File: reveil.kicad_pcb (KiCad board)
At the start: 2 copper layers, 170 x 90 mm, 31 parts, among them J1 Barrel_Jack_Switch, J2 AudioJack3_SwitchTR, Q1 2N3904, Q2 IRF540N, U1 MAX7219, U2 MAX7219

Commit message: Mise à jour du layout PCB
Co-Authored-By: Claude Sonnet 5 <noreply@anthropic.com>
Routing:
- net ARRET_ALARME: track 166.8 -> 171.3 mm
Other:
- board text added: "+3V3"
- board text added: "ALARME_ON_OFF"
- board text added: "ARRET_ALARME"
- board text added: "DATE_CLK"
- board text added: "DATE_DIN"
- board text added: "DATE_LOAD"
- board text added: "GND"
- board text added: "H_ALRM_CLK"
- board text added: "H_ALRM_DIN"
- board text added: "H_ALRM_LD"
- board text added: "LED"
- board text added: "LUMIERE"
- board text added: "LUMINOSITE"
- board text added: "REG_ALRM_A"
- board text added: "REG_ALRM_B"
- board text added: "REG_ALRM_S"
- board text added: "REG_DATE_A"
- board text added: "REG_DATE_B"
- board text added: "REG_DATE_S"
- board text added: "REG_HR_A"
- board text added: "REG_HR_B"
- board text added: "REG_HR_S"
- board text added: "Réveil pour sourd Oscar Lederrey V1.1"
- board text added: "VBUS"
- board text added: "VIBREUR"
- board text removed: "Réveil pour sourd Oscar Lederrey V1.0"

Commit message: Corrige le pinout du footprint du switch ALARME_ON_OFF1 (court-circuit GND/+3V3)
Le footprint système Button_Switch_THT:SW_Slide-03_Wuerth-WS-SLTV a
les pads 1 et 2 physiquement inversés par rapport au composant monté
(pin 1 attendu à gauche, pin 2 au centre — le footprint avait
l'inverse). Résultat : selon la position du switch, +3V3 et GND se
retrouvaient court-circuités via l'interrupteur, faisant chauffer le
Pico et les câbles d'alimentation.

Correctif : nouvelle librairie locale reveil.pretty/ avec une copie
du footprint où seuls les pads 1 et 2 échangent leur géométrie (même
taille/forme/perçage, juste la position), enregistrée via
fp-lib-table. Le schéma (ALARME_ON_OFF1) et le PCB référencent
maintenant reveil:SW_Slide-03_... ; les pistes ont été reroutées en
conséquence.

Confirmé par :
- Mesure au multimètre (court quasi 0 Ω entre GND et +3V3, reproduit
  en rebranchant ces deux fils) ayant permis d'identifier la cause
- ERC propre (0 erreur/avertissement)
- DRC propre après routage (plus de shorting_items ni de pad non
  connecté sur ALARME_ON_OFF1)

Co-Authored-By: Claude Sonnet 5 <noreply@anthropic.com>
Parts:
- ALARME_ON_OFF1: footprint Button_Switch_THT:SW_Slide-03_Wuerth-WS-SLTV_10x2.5x6.4_P2.54mm -> reveil:SW_Slide-03_Wuerth-WS-SLTV_10x2.5x6.4_P2.54mm
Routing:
- net +3V3: track 171.7 -> 182.7 mm
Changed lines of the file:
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@@
 		)
 	)
-	(footprint "Button_Switch_THT:SW_Slide-03_Wuerth-WS-SLTV_10x2.5x6.4_P2.54mm"
+	(footprint "reveil:SW_Slide-03_Wuerth-WS-SLTV_10x2.5x6.4_P2.54mm"
 		(layer "F.Cu")
 		(at 196.46 90.5 180)
@@
 			)
 		)
-		(pad "1" thru_hole rect
-			(at 0 0 180)
-			(size 1.5 1.5)
+		(pad "1" thru_hole circle
+			(at -2.54 0 180)
+			(size 1.6 1.6)
 			(drill 0.8)
 			(layers "*.Cu" "*.Mask")
@@
 			(pintype "passive")
 		)
-		(pad "2" thru_hole circle
-			(at -2.54 0 180)
-			(size 1.6 1.6)
+		(pad "2" thru_hole rect
+			(at 0 0 180)
+			(size 1.5 1.5)
 			(drill 0.8)
 			(layers "*.Cu" "*.Mask")
@@
 	(segment
 		(start 197.321 88.821)
-		(end 199 90.5)
+		(end 196.46 90.5)
 		(width 0.2)
 		(layer "B.Cu")
@@
 	)
 	(segment
+		(start 191.4655 85.5055)
+		(end 191.4655 92.4655)
+		(width 0.2)
+		(layer "B.Cu")
+		(net 28)
+	)
+	(segment
 		(start 140.4925 85.1882)
 		(end 141.0978 85.7935)
@@
 	)
 	(segment
+		(start 193 94)
+		(end 198 94)
+		(width 0.2)
+		(layer "B.Cu")
+		(net 28)
+	)
+	(segment
 		(start 132.9578 59.1761)
 		(end 140.4925 66.7108)
@@
 	)
 	(segment
+		(start 191.4655 92.4655)
+		(end 193 94)
+		(width 0.2)
+		(layer "B.Cu")
+		(net 28)
+	)
+	(segment
 		(start 132.9578 55.2865)
 		(end 132.9578 59.1761)
@@
 	)
 	(segment
+		(start 199 93)
+		(end 199 90.5)
+		(width 0.2)
+		(layer "B.Cu")
+		(net 28)
+	)
+	(segment
 		(start 140.2231 37.2731)
 		(end 140.2231 48.0212)
@@
 	)
 	(segment
-		(start 140.4925 66.7108)
-		(end 140.4925 85.1882)
+		(start 198 94)
+		(end 199 93)
 		(width 0.2)
 		(layer "B.Cu")
@@
 	)
 	(segment
-		(start 140.2231 48.0212)
-		(end 132.9578 55.2865)
+		(start 140.4925 66.7108)
+		(end 140.4925 85.1882)
 		(width 0.2)
 		(layer "B.Cu")
@@
 	)
 	(segment
-		(start 191.4655 85.5055)
-		(end 196.46 90.5)
+		(start 140.2231 48.0212)
+		(end 132.9578 55.2865)
 		(width 0.2)
 		(layer "B.Cu")

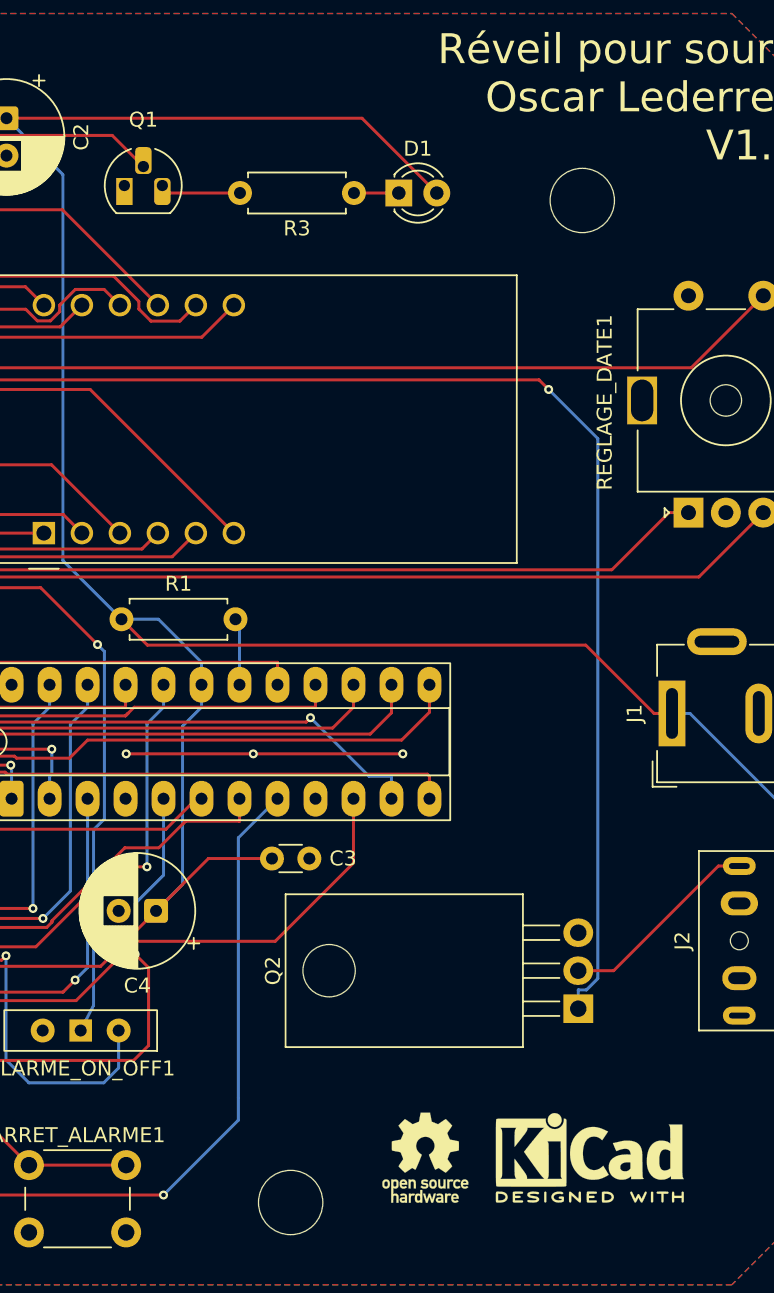
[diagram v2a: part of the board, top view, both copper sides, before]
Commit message: Place et route R4 sur le PCB (résistance de base LED)
R4 (1.5 kΩ, ajoutée au schéma dans le commit précédent) est
maintenant placée et routée sur le PCB. reveil.kicad_sch est
reformaté par KiCad (réordonnancement interne des blocs, aucun
changement électrique) suite à la synchronisation schéma/PCB.

Vérifié par ERC (0 erreur/avertissement) et DRC (0 pad non connecté,
0 erreur de footprint ; seuls restent des avertissements
silk_edge_clearance préexistants sur J2, sans rapport avec ce fix).

Test fonctionnel de la LED pas encore fait : une correction PCB
supplémentaire est nécessaire avant de pouvoir tester (voir TODO
README).

Co-Authored-By: Claude Sonnet 5 <noreply@anthropic.com>
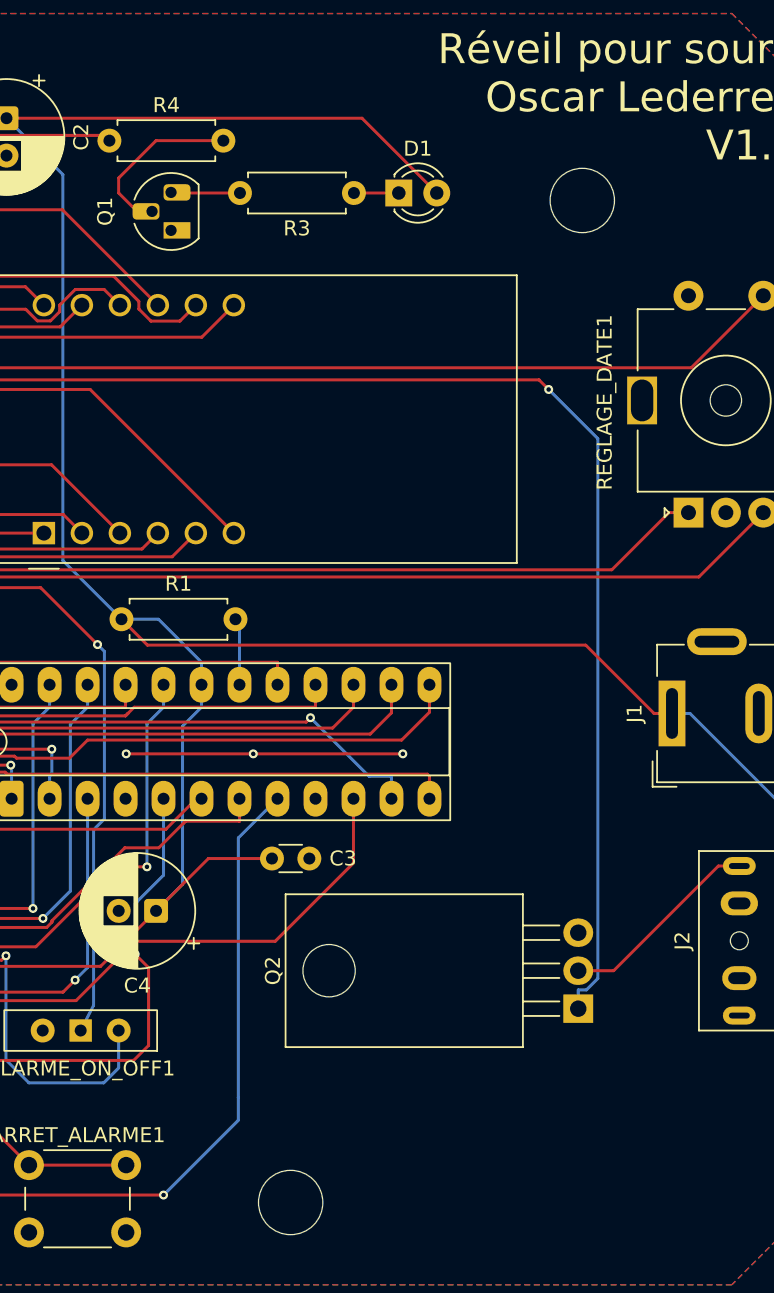
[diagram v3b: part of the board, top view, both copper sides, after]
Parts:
- removed LOGO1: OSHW-Logo_5.7x6mm_SilkScreen, Symbol:OSHW-Logo_5.7x6mm_SilkScreen
- removed LOGO2: KiCad-Logo2_5mm_SilkScreen, Symbol:KiCad-Logo2_5mm_SilkScreen
- added R4: 1.5K, Resistor_THT:R_Axial_DIN0207_L6.3mm_D2.5mm_P7.62mm_Horizontal, F.Cu at (198.4, 31.0)
- R3: value R -> 100
- moved Q1 4.33 mm to (202.5, 37.0), turned to 90 degrees
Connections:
- Q1 pad 2: LED -> Net-(Q1-B)
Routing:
- net Net-(Q1-B): track 0.00 -> 11.8 mm
- net LED: track 123.8 -> 120.8 mm
- net Net-(Q1-C): track 5.40 -> 4.63 mm

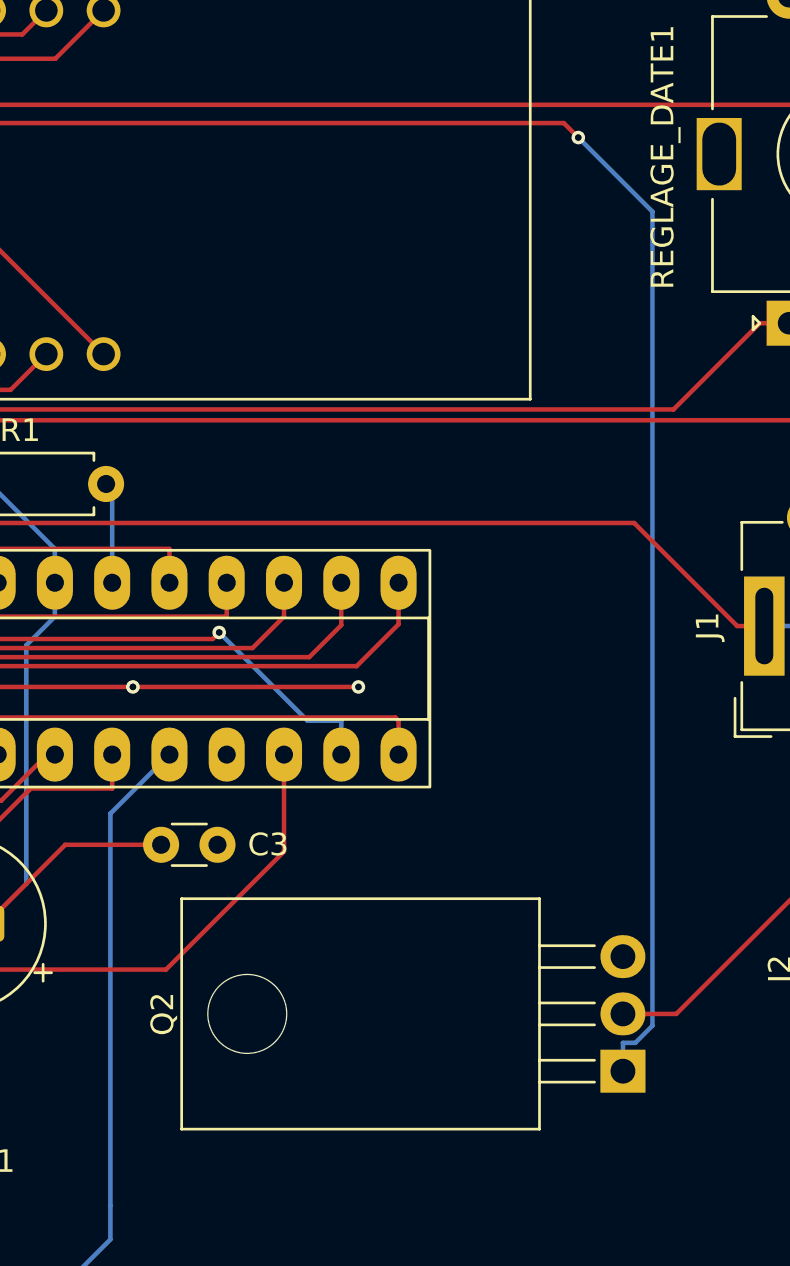
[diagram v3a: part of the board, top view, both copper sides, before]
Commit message: Remplace Q2 (IRF510/IRF540N) par un IRLB8721PbF logic-level et ajoute R5
Le RP2040 pilote la grille de Q2 directement en 3.3V (GP18), et ni
l'IRF510 (carte physique) ni l'IRF540N (schéma) ne sont des MOSFET
logic-level (Rds(on) specifie a Vgs=10V) : risque de sous-enhancement
et d'echauffement. L'IRLB8721PbF est pleinement enhance des 2.5-4.5V,
compatible avec un pilotage direct en 3.3V.

Ajoute R5 = 100 ohm en serie entre GP18 et la grille de Q2 pour
limiter le pic de courant transitoire et amortir le ringing.

Verifie : pinout G/D/S (broches 1/2/3, meme convention que l'IRF540N),
footprint TO-220-3_Horizontal_TabDown (corrige apres reperage d'un
TO-220F errone), ERC (0 violation) et DRC (6 avertissements
preexistants sur J2, sans rapport).

Co-Authored-By: Claude Sonnet 5 <noreply@anthropic.com>
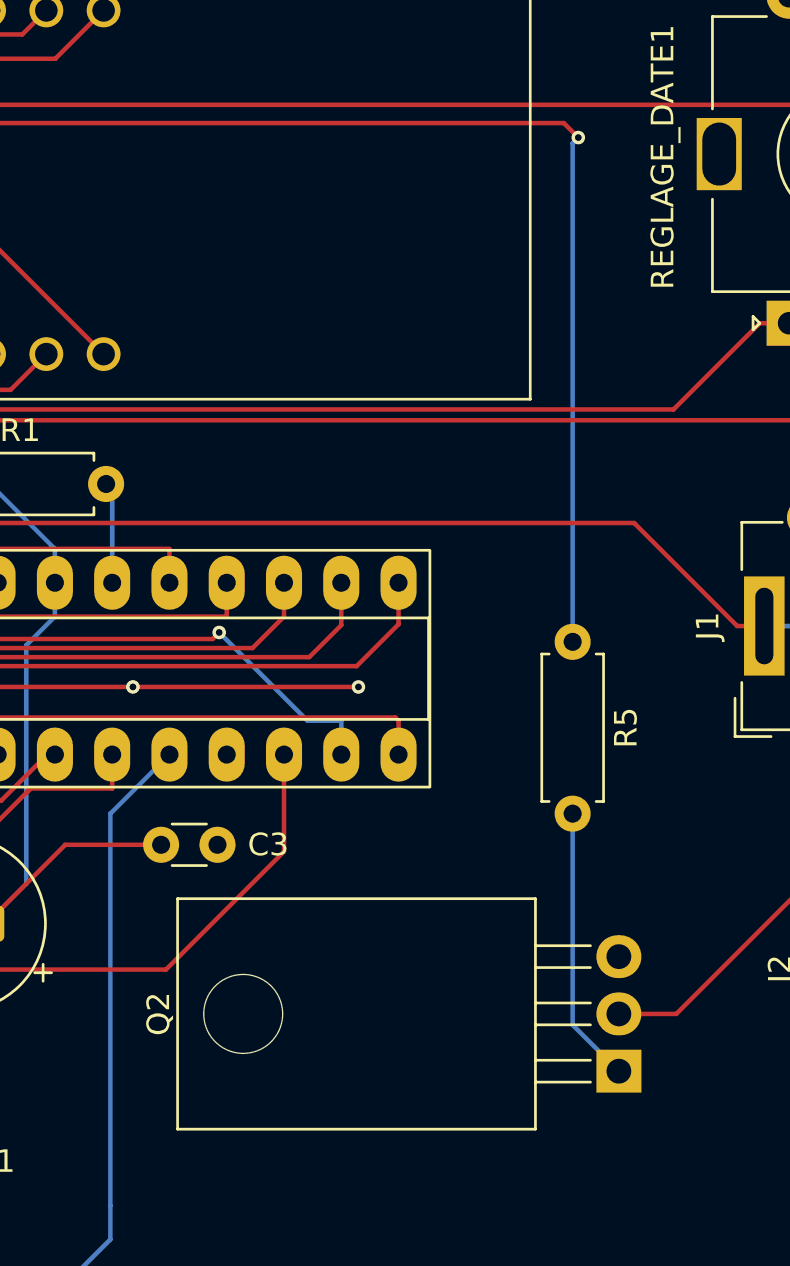
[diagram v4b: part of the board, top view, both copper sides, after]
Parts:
- added R5: 100R, Resistor_THT:R_Axial_DIN0207_L6.3mm_D2.5mm_P7.62mm_Horizontal, F.Cu at (227.5, 70.0)
- Q2: value IRF540N -> IRLB8721PBF
- moved Q2 0.18 mm to (229.6, 89.0)
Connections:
- Q2 pad 1: VIBREUR -> Net-(Q2-G)
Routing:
- net VIBREUR: track 190.1 -> 169.0 mm
- net Net-(Q2-G): track 0.00 -> 12.3 mm

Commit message: Schéma/PCB : remplace le symbole des afficheurs CA56-12EWA par CC56-12EWA
Le schéma utilisait un symbole à anode commune alors que le câblage
(anodes communes CA1-CA4 vers les sorties DIG_x du MAX7219, qui
absorbent le courant) n'a de sens qu'avec des afficheurs à cathode
commune. Comme le circuit fonctionne, les composants montés sont bien
des CC56-12EWA.

Remplace le symbole dans date.kicad_sch et heure_alarme.kicad_sch (les
4 instances DATE1/ANNEE1/HEURE1/ALARME1), ainsi que la Value des
empreintes correspondantes dans reveil.kicad_pcb. Le footprint
(Display_7Segment:CA56-12EWA) et le datasheet sont inchangés : même
brochage, seules la doc et la BOM changent.

ERC/DRC revérifiés via le conteneur Docker KiBot : 0 erreur/avertissement
ERC, 6 avertissements DRC silk_edge_clearance sur J2 (inchangé,
préexistant), 0 écart schéma/PCB.

Co-Authored-By: Claude Sonnet 5 <noreply@anthropic.com>
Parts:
- ALARME1, ANNEE1, DATE1, HEURE1: value CA56-12EWA -> CC56-12EWA

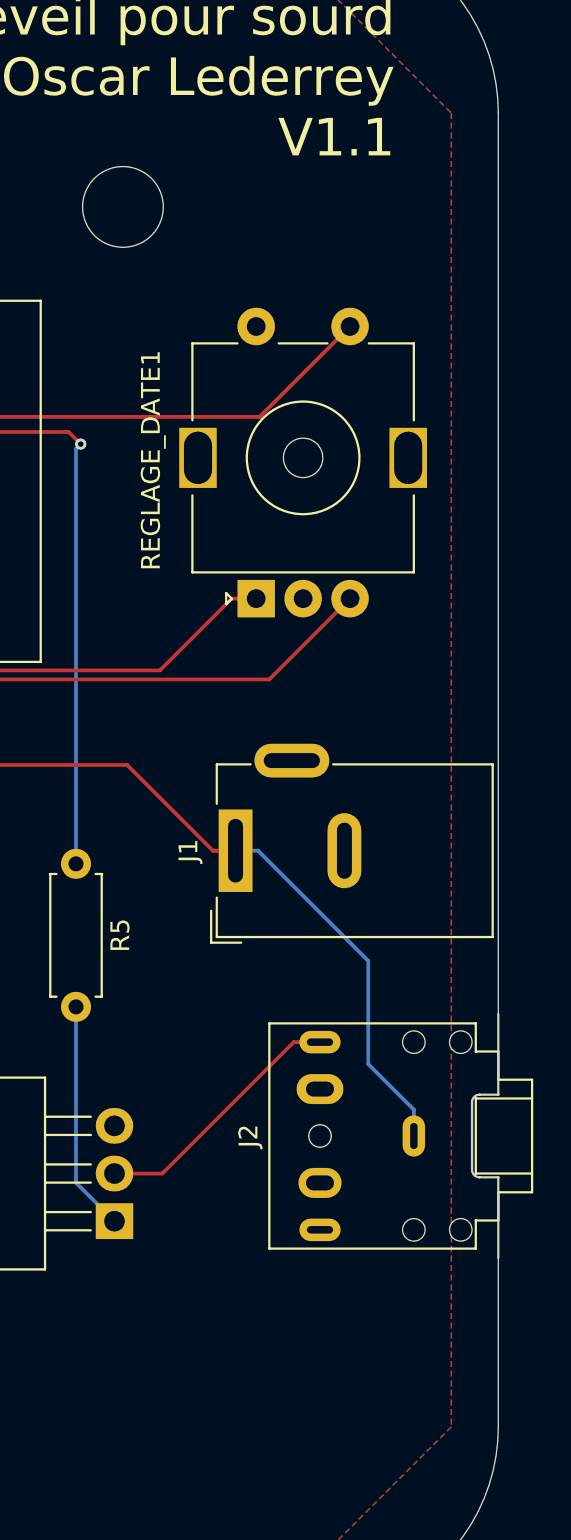
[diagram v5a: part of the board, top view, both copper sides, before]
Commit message: Schéma/PCB : ajoute la diode de roue libre et le snubber du moteur
Rien ne protégeait le drain de Q2 contre la surtension inductive à la
coupure du moteur M1 (roue libre) : l'avalanche de Q2 absorbait
l'énergie et parasitait le 5 V du Pico.

Ajoute en parallèle de M1, entre le drain de Q2 et VBUS :
- D2 (Schottky 1N5819), cathode côté VBUS, anode côté drain de Q2
- C5 (100 nF) contre les parasites de commutation des balais du moteur

Empreintes placées et pistes routées sur le PCB ; schéma réorganisé
pour la lisibilité.

Connectivité vérifiée via le netlist KiCad (D2 cathode sur le net VBUS,
D2 anode + C5 sur le même net que le drain de Q2 / M1) et ERC/DRC
revérifiés via le conteneur Docker KiBot : 0 erreur/avertissement ERC ;
DRC revenu à la référence (6 avertissements silk_edge_clearance
préexistants sur J2), aucun écart schéma/PCB.

Co-Authored-By: Claude Sonnet 5 <noreply@anthropic.com>
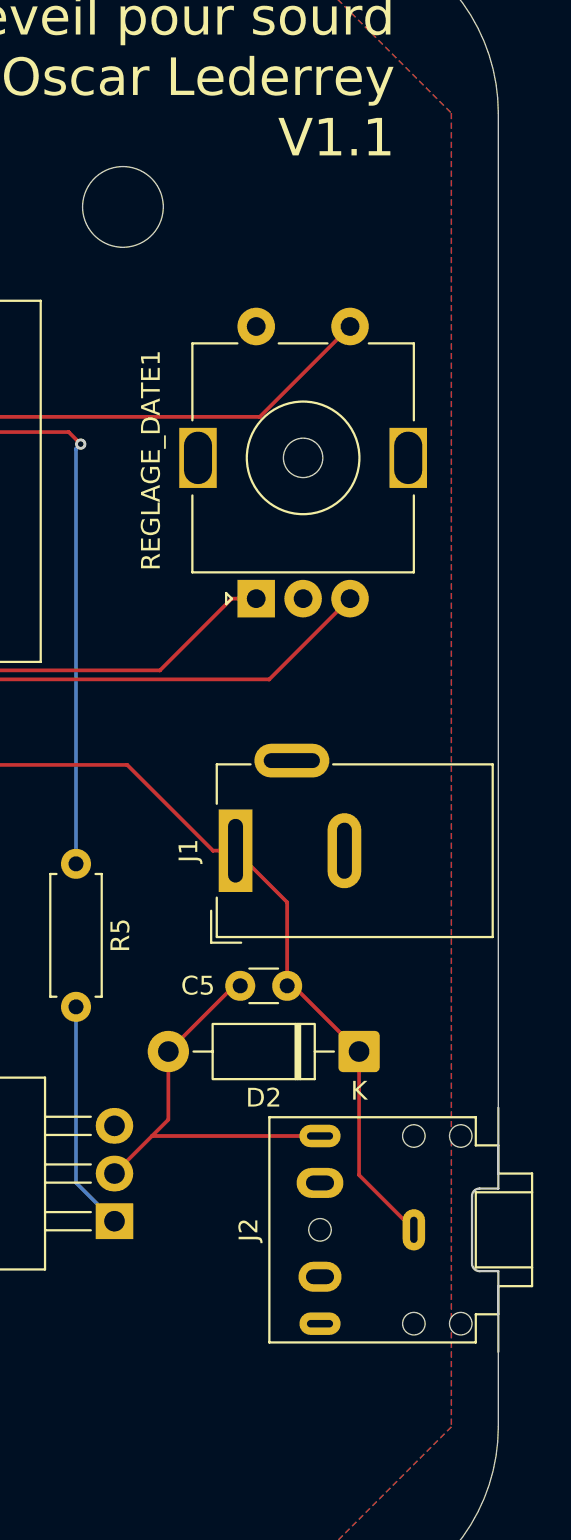
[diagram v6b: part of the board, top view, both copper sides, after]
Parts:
- added C5: 100n, Capacitor_THT:C_Disc_D3.0mm_W1.6mm_P2.50mm, F.Cu at (238.8, 76.5)
- added D2: 1N5819, Diode_THT:D_DO-41_SOD81_P10.16mm_Horizontal, F.Cu at (242.6, 80.0)
- moved J2 5.00 mm to (245.5, 89.5)
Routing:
- net Net-(D2-A): track 13.7 -> 21.9 mm
- net VBUS: track 322.7 -> 327.2 mm
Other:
- outline, holes or cut-outs redrawn
